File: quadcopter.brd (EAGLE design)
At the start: 138 x 138 mm, 65 parts, among them J1 AVR_SPI_PRG_6NS, Q1 N-CHANNEL_MOSFET, Q2 N-CHANNEL_MOSFET, Q3 N-CHANNEL_MOSFET, Q4 N-CHANNEL_MOSFET, U1 ATMEGA128RFA1

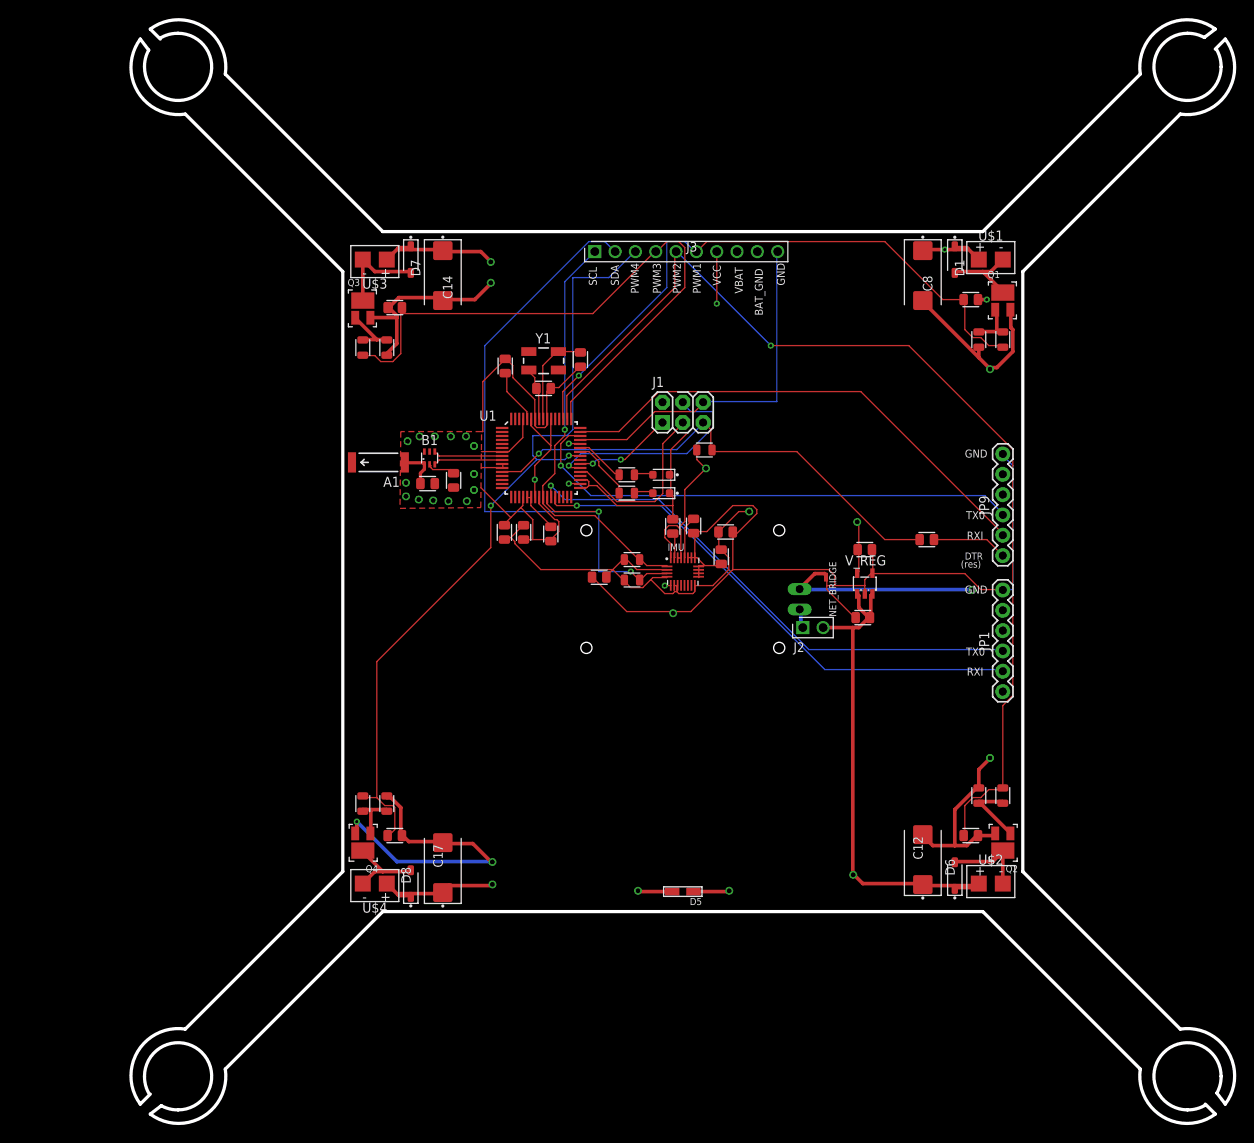
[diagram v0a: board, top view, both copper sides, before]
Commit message: Made most of swanson changes. Did not add reset button yet and did not autoroute and did not add in holes yet
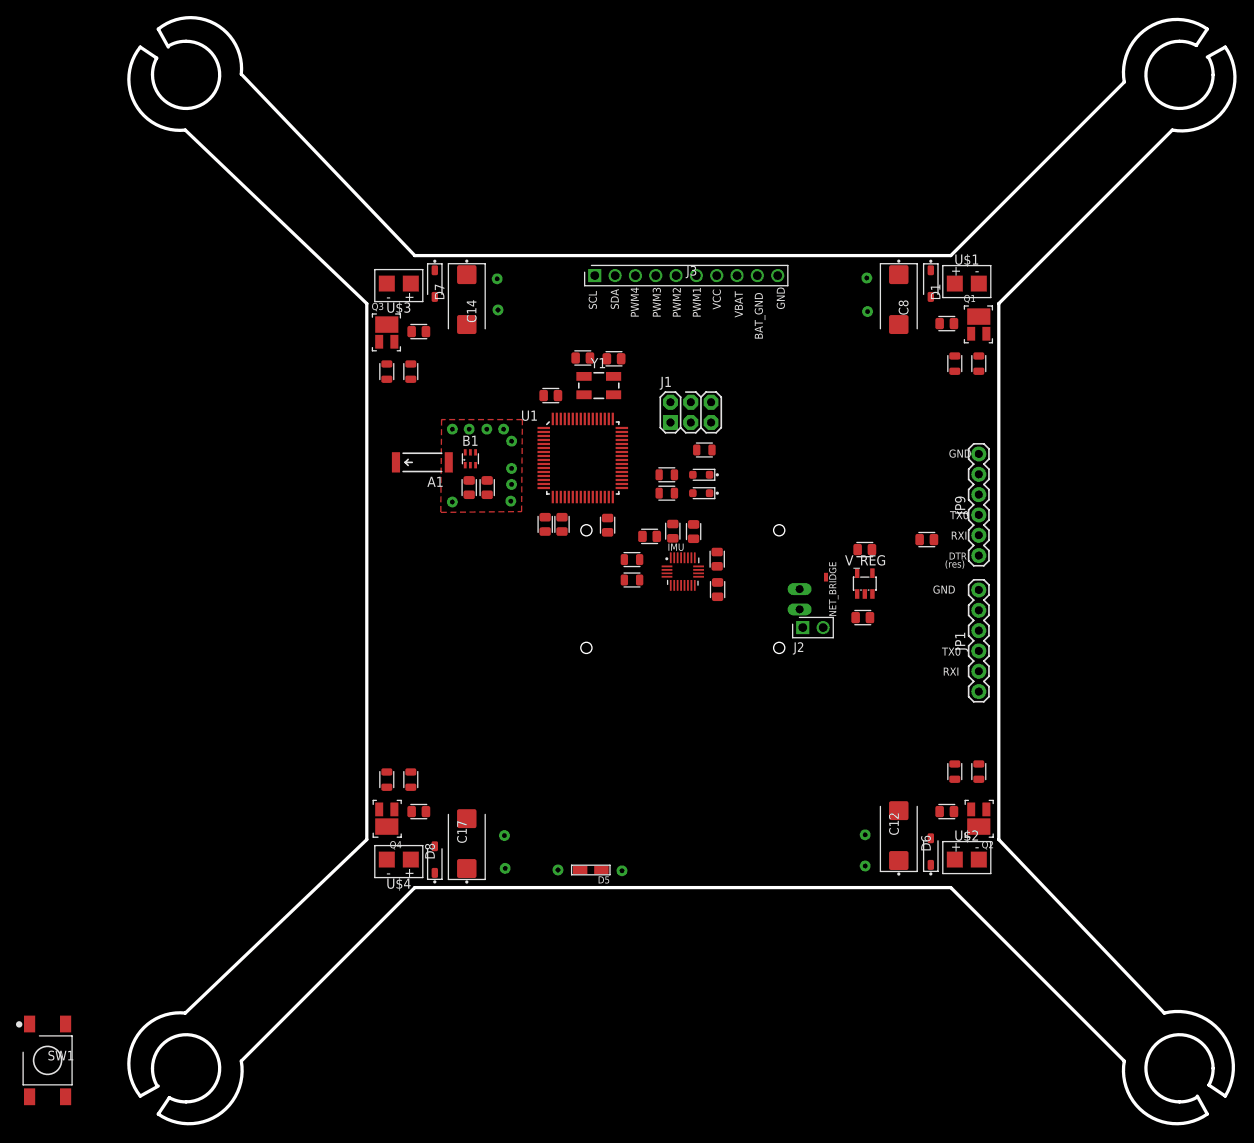
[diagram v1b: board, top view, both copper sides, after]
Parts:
- added SW1: PUSHBUTTON_SMD-VERTICAL-1, quadparts_prebuilt:TE_FSM8JSMA_HS
- moved D5 11.8 mm to (58.5, 32.7)
- moved C3 10.5 mm to (60.6, 75.8), turned to 270 degrees
- moved C22 8.11 mm to (65.8, 74.4)
- moved Y1 7.56 mm to (59.5, 93.2)
- moved C20 7.27 mm to (74.3, 67.8), turned to 90 degrees
- moved C4 7.27 mm to (54.9, 75.9)
- moved C1 6.80 mm to (53.5, 92.0), turned to 180 degrees
- moved C5 6.20 mm to (57.5, 96.7)
- moved A1 5.50 mm to (37.5, 83.7)
- moved C9 5.22 mm to (43.3, 80.5), turned to 90 degrees
- moved U1 5.20 mm to (57.5, 84.2)
- moved B1 5.10 mm to (43.5, 84.1)
- moved LED2 5.00 mm to (72.3, 82.1)
- moved LED3 5.00 mm to (72.3, 79.8)
- moved R5 5.00 mm to (68.0, 79.8)
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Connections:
- net BAT_GND: now also R10.1, R2.1, R4.1, R8.2; no longer C10.2, C13.2, C16.2, C7.2
- net FILTERED1: now also C7.2; no longer R2.2
- net FILTERED2: now also C10.2; no longer R4.2
- net FILTERED3: now also C13.2; no longer R8.2
- net FILTERED4: now also C16.2; no longer R10.2
- net PWM1: now also R2.2; no longer R2.1
- net PWM2: now also R4.2; no longer R4.1
- net PWM4: now also R10.2; no longer R10.1
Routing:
- net GND: track 264.8 -> 0.00 mm, vias 16 -> 0
- net BAT_GND: track 141.6 -> 0.00 mm, vias 8 -> 5
- net PWM2: track 131.5 -> 0.00 mm, vias 1 -> 0
- net VCC: track 111.9 -> 0.00 mm, vias 7 -> 0
- net VBAT: track 110.8 -> 0.00 mm
- net PWM4: track 101.6 -> 0.00 mm, vias 2 -> 0
- net SDA: track 81.7 -> 0.00 mm, vias 2 -> 0
- net PWM1: track 78.4 -> 0.00 mm, vias 1 -> 0
- net PWM3: track 78.3 -> 0.00 mm
- net N$9: track 66.6 -> 0.00 mm, vias 1 -> 0
- net N$12: track 65.6 -> 0.00 mm, vias 1 -> 0
- net RX0: track 63.5 -> 0.00 mm, vias 1 -> 0
- net TX0: track 62.5 -> 0.00 mm
- net RESET: track 62.3 -> 0.00 mm, vias 1 -> 0
- net SCL: track 53.0 -> 0.00 mm, vias 1 -> 0
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- added copper zone on layer 15, net N$22
- added copper zone on layer 2, net N$22
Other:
- board size 138 x 138 mm -> 138.3 x 138.3 mm

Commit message: added reset button and did autorouting
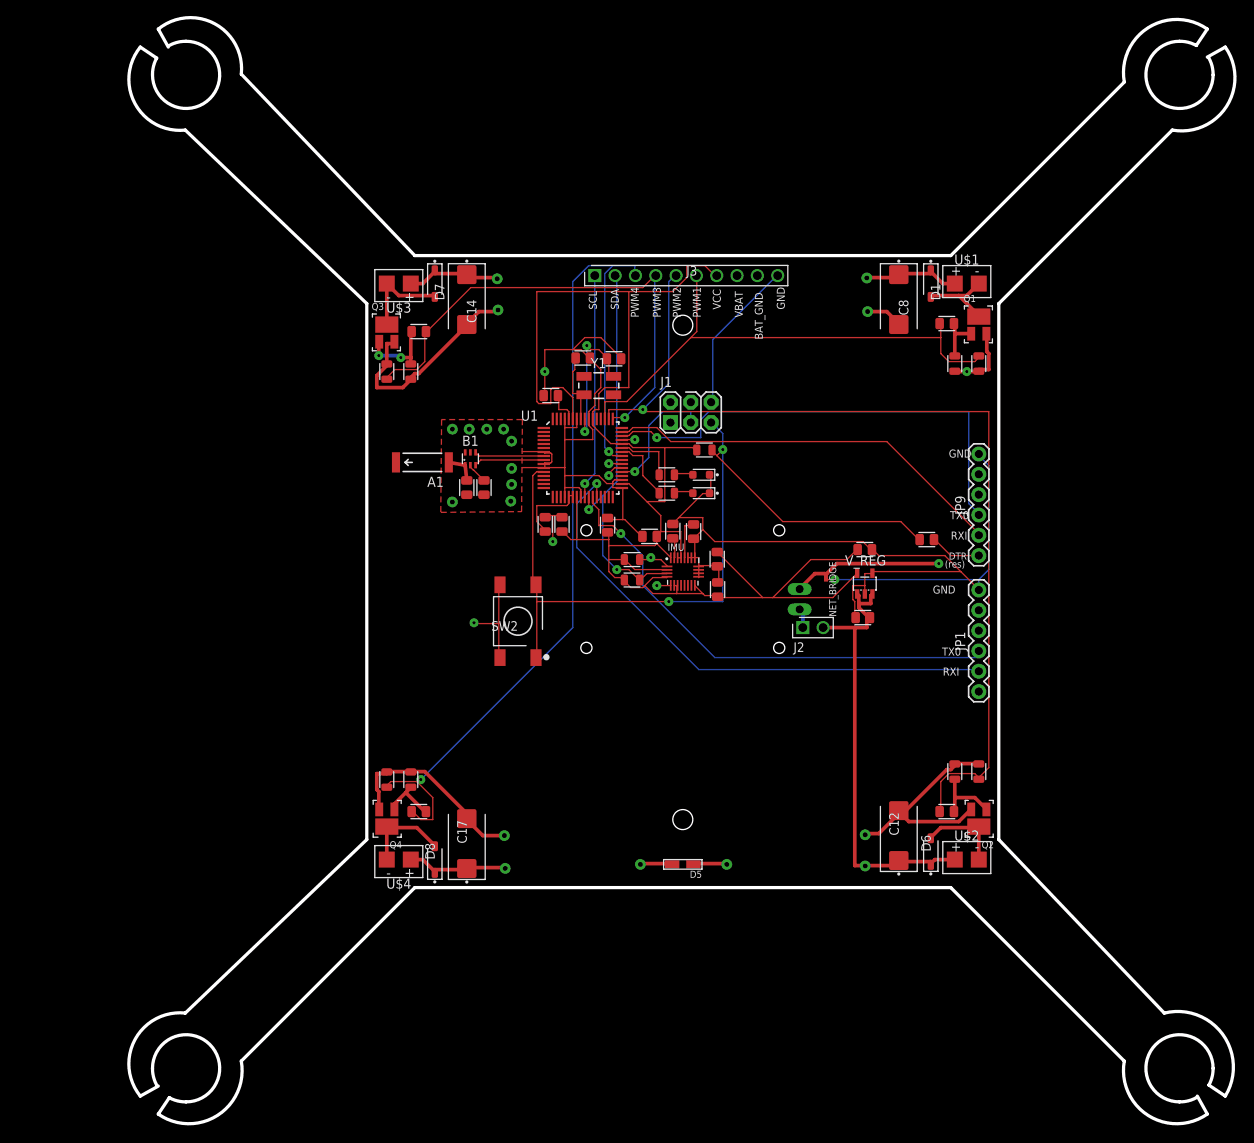
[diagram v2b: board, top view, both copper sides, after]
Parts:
- removed SW1: PUSHBUTTON_SMD-VERTICAL-1, quadparts_prebuilt:TE_FSM8JSMA_HS
- added SW2: PUSHBUTTON_SMD-VERTICAL-1, quadparts_prebuilt:TE_FSM8JSMA_HS
- moved D5 11.5 mm to (70.0, 33.4)
- moved C11 0.40 mm to (45.1, 80.5)
- moved C9 0.30 mm to (43.0, 80.5), turned to 270 degrees
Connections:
- net GND: now also SW2.3, SW2.4
- net RESET: now also SW2.1, SW2.2
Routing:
- net GND: track 0.00 -> 244.3 mm, vias 0 -> 6
- net VCC: track 0.00 -> 203.2 mm
- net PWM2: track 0.00 -> 123.1 mm, vias 0 -> 1
- net PWM4: track 0.00 -> 119.2 mm, vias 0 -> 2
- net BAT_GND: track 0.00 -> 116.8 mm, vias 5 -> 7
- net RESET: track 0.00 -> 102.7 mm, vias 0 -> 2
- net VBAT: track 0.00 -> 99.7 mm
- net N$12: track 0.00 -> 67.5 mm, vias 0 -> 1
- net PWM1: track 0.00 -> 65.1 mm
- net PWM3: track 0.00 -> 62.4 mm, vias 0 -> 1
- net N$9: track 0.00 -> 61.2 mm, vias 0 -> 1
- net RX0: track 0.00 -> 60.0 mm, vias 0 -> 1
- net TX0: track 0.00 -> 50.5 mm
- net SDA: track 0.00 -> 49.6 mm, vias 0 -> 2
- net SCL: track 0.00 -> 44.9 mm, vias 0 -> 2
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
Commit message: Made all changes specified in design review. Except LED
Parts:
- moved C9 1.81 mm to (41.2, 80.7)
- moved C11 1.61 mm to (43.5, 80.7)
- moved A1 0.70 mm to (37.5, 84.3)
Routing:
- net N$6: track 18.6 -> 9.48 mm, vias 2 -> 0
- net SCL: track 44.9 -> 51.9 mm
- net SDA: track 49.6 -> 53.0 mm
- net PWM4: track 119.2 -> 122.5 mm
- net N$8: track 3.99 -> 4.70 mm
- net N$1: track 9.64 -> 8.94 mm
- net N$7: track 2.63 -> 2.05 mm
- net GND: track 244.3 -> 244.0 mm, vias 6 -> 7
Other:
- board size 138.3 x 138.3 mm -> 138.5 x 138.5 mm

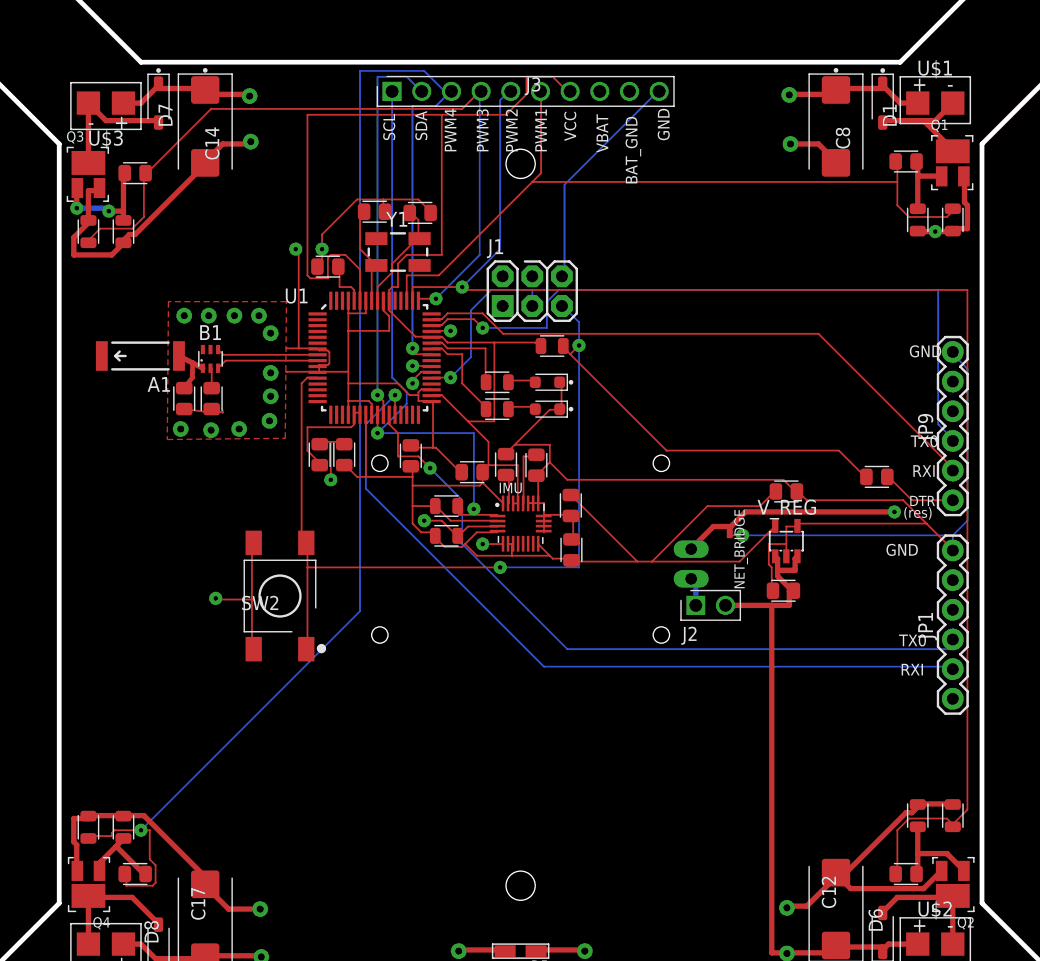
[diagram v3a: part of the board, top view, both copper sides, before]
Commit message: Changed the resistor and capacitor placements in the motor drivers
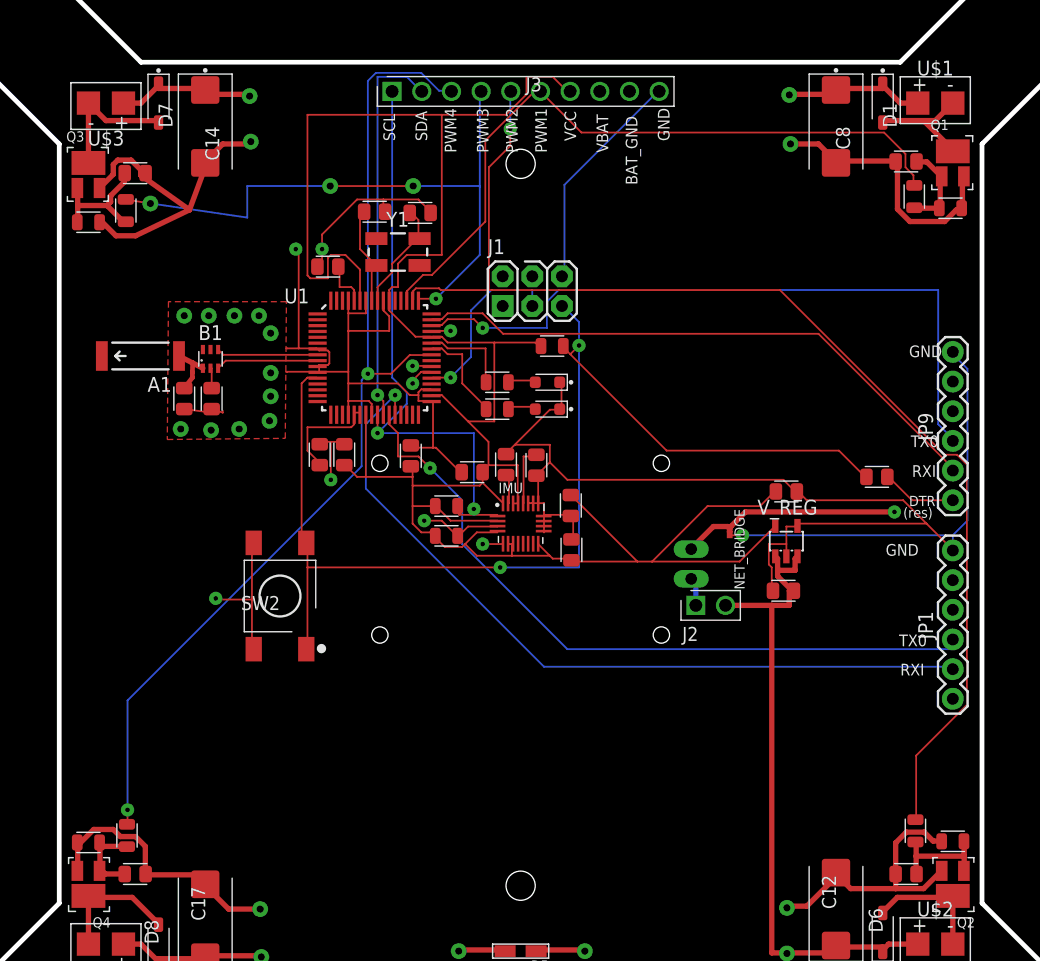
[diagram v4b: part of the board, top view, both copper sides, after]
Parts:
- moved R2 3.86 mm to (103.7, 98.0)
- moved R7 3.72 mm to (107.0, 42.8), turned to 0 degrees
- moved R8 3.67 mm to (36.2, 96.8)
- moved R4 3.45 mm to (103.8, 43.7), turned to 90 degrees
- moved R10 3.37 mm to (36.3, 43.3)
- moved R11 3.27 mm to (33.0, 42.7), turned to 0 degrees
- moved R9 3.10 mm to (33.0, 95.8), turned to 180 degrees
- moved R3 2.97 mm to (106.8, 97.0), turned to 180 degrees
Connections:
- net BAT_GND: now also C10.1, C13.1, C16.2, C7.1; no longer R10.1, R2.1, R4.1, R8.2
- net FILTERED1: now also R2.1
- net FILTERED2: now also R4.1
- net FILTERED3: now also R8.1
- net FILTERED4: now also C16.1, R10.2; no longer C16.2
- net PWM1: no longer C7.1
- net PWM2: no longer C10.1
- net PWM3: now also R8.2; no longer C13.1, R8.1
- net PWM4: now also R10.1; no longer C16.1, R10.2
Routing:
- net PWM4: track 122.5 -> 86.4 mm
- net PWM2: track 123.1 -> 104.6 mm
- net PWM3: track 62.4 -> 54.2 mm, vias 1 -> 4
- net BAT_GND: track 116.8 -> 122.8 mm, vias 7 -> 6
- net PWM1: track 65.1 -> 59.9 mm
- net FILTERED1: track 6.20 -> 7.65 mm
- net FILTERED3: track 10.1 -> 11.1 mm, vias 2 -> 0
- net FILTERED2: track 8.72 -> 9.45 mm
